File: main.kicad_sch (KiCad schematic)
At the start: 11 parts, among them J101 Conn_Coaxial, U101 SA818V

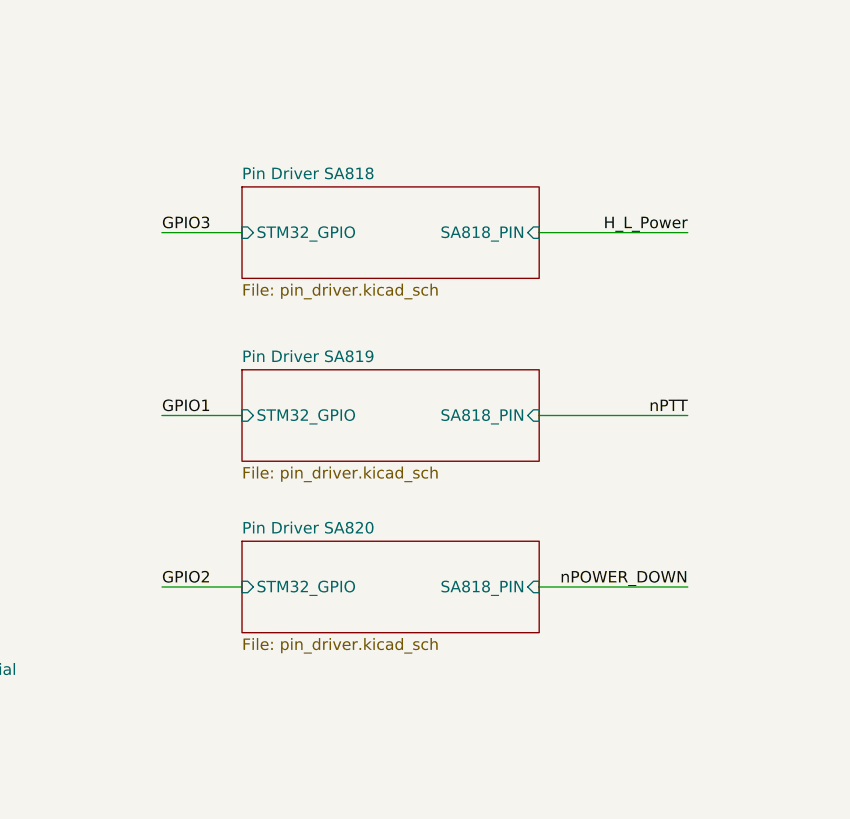
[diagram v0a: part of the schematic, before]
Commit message: update stm32, add some new 3d files
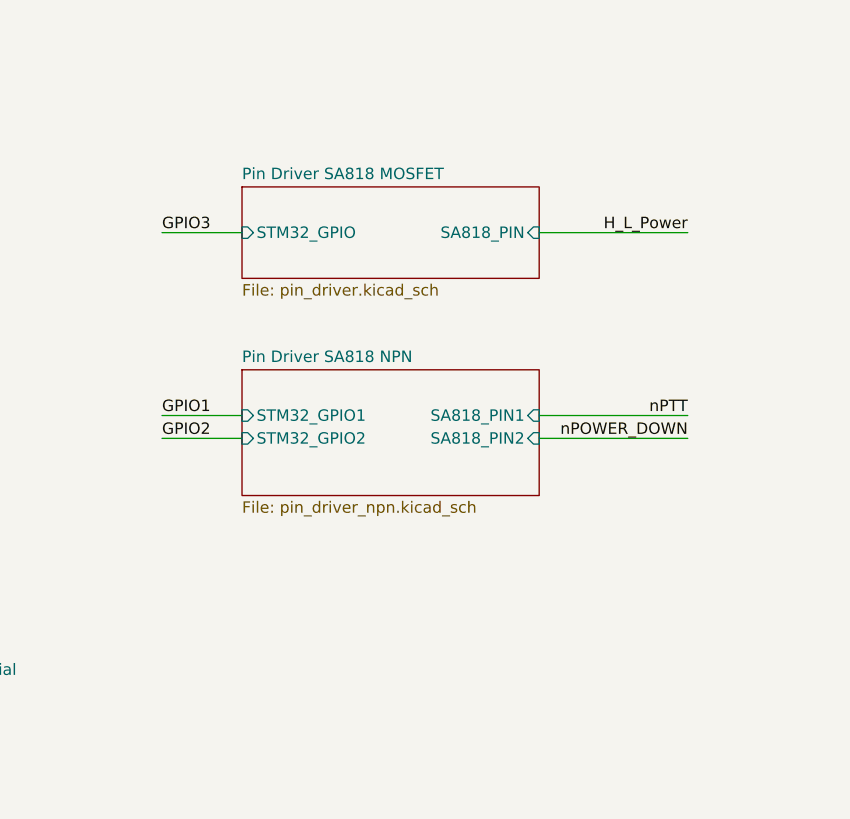
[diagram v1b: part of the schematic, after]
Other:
- sheet Pin Driver SA818 renamed Pin Driver SA818 MOSFET
- removed sheet Pin Driver SA819
- removed sheet Pin Driver SA820
- added sheet Pin Driver SA818 NPN (pin_driver_npn.kicad_sch)
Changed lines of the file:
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@@
 	(wire
 		(pts
-			(xy 158.75 144.78) (xy 175.26 144.78)
+			(xy 158.75 128.27) (xy 175.26 128.27)
 		)
 		(stroke
@@
 	(wire
 		(pts
-			(xy 116.84 144.78) (xy 125.73 144.78)
+			(xy 116.84 128.27) (xy 125.73 128.27)
 		)
 		(stroke
@@
 	)
 	(label "nPOWER_DOWN"
-		(at 175.26 144.78 180)
+		(at 175.26 128.27 180)
 		(effects
 			(font
@@
 	)
 	(label "GPIO2"
-		(at 116.84 144.78 0)
+		(at 116.84 128.27 0)
 		(effects
 			(font
@@
 	)
 	(sheet
-		(at 125.73 139.7)
-		(size 33.02 10.16)
-		(exclude_from_sim no)
-		(in_bom yes)
-		(on_board yes)
-		(dnp no)
-		(fields_autoplaced yes)
-		(stroke
-			(width 0.1524)
-			(type solid)
-		)
-		(fill
-			(color 0 0 0 0.0000)
-		)
-		(property "Sheetname" "Pin Driver SA820"
-			(at 125.73 138.9884 0)
-			(effects
-				(font
-					(size 1.27 1.27)
-				)
-				(justify left bottom)
-			)
-		)
-		(property "Sheetfile" "pin_driver.kicad_sch"
-			(at 125.73 150.4446 0)
-			(effects
-				(font
-					(size 1.27 1.27)
-				)
-				(justify left top)
-			)
-		)
-		(pin "SA818_PIN" input
-			(at 158.75 144.78 0)
-			(effects
-				(font
-					(size 1.27 1.27)
-				)
-				(justify right)
-			)
-		)
-		(pin "STM32_GPIO" input
-			(at 125.73 144.78 180)
-			(effects
-				(font
-					(size 1.27 1.27)
-				)
-				(justify left)
-			)
-		)
-		(instances
-			(project "fm"
-				(path "/f228839c-6576-40b2-ae70-679b7b460639"
-					(page "7")
-				)
-			)
-		)
-	)
-	(sheet
 		(at 125.73 100.33)
 		(size 33.02 10.16)
@@
 			(color 0 0 0 0.0000)
 		)
-		(property "Sheetname" "Pin Driver SA818"
+		(property "Sheetname" "Pin Driver SA818 MOSFET"
 			(at 125.73 99.6184 0)
 			(effects
@@
 		)
 		(instances
-			(project "fm"
+			(project "main"
 				(path "/f228839c-6576-40b2-ae70-679b7b460639"
 					(page "5")
@@
 		)
 		(instances
-			(project "fm"
+			(project "main"
 				(path "/f228839c-6576-40b2-ae70-679b7b460639"
 					(page "4")
@@
 	(sheet
 		(at 125.73 120.65)
-		(size 33.02 10.16)
+		(size 33.02 13.97)
 		(exclude_from_sim no)
 		(in_bom yes)
@@
 			(color 0 0 0 0.0000)
 		)
-		(property "Sheetname" "Pin Driver SA819"
+		(property "Sheetname" "Pin Driver SA818 NPN"
 			(at 125.73 119.9384 0)
 			(effects
@@
 			)
 		)
-		(property "Sheetfile" "pin_driver.kicad_sch"
-			(at 125.73 131.3946 0)
+		(property "Sheetfile" "pin_driver_npn.kicad_sch"
+			(at 125.73 135.2046 0)
 			(effects
 				(font
@@
 			)
 		)
-		(pin "SA818_PIN" input
+		(pin "SA818_PIN1" input
 			(at 158.75 125.73 0)
 			(effects
@@
 			)
 		)
-		(pin "STM32_GPIO" input
+		(pin "SA818_PIN2" input
+			(at 158.75 128.27 0)
+			(effects
+				(font
+					(size 1.27 1.27)
+				)
+				(justify right)
+			)
+		)
+		(pin "STM32_GPIO1" input
 			(at 125.73 125.73 180)
 			(effects
@@
 			)
 		)
-		(instances
-			(project "fm"
-				(path "/f228839c-6576-40b2-ae70-679b7b460639"
-					(page "6")
+		(pin "STM32_GPIO2" input
+			(at 125.73 128.27 180)
+			(effects
+				(font
+					(size 1.27 1.27)
+				)
+				(justify left)
+			)
+		)
+		(instances
+			(project "main"
+				(path "/f228839c-6576-40b2-ae70-679b7b460639"
+					(page "7")
 				)
 			)
@@
 		)
 		(instances
-			(project "fm"
+			(project "main"
 				(path "/f228839c-6576-40b2-ae70-679b7b460639"
 					(page "8")
@@
 		)
 		(instances
-			(project "fm"
+			(project "main"
 				(path "/f228839c-6576-40b2-ae70-679b7b460639"
 					(page "3")
@@
 		)
 		(instances
-			(project "fm"
+			(project "main"
 				(path "/f228839c-6576-40b2-ae70-679b7b460639"
 					(page "2")

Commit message: add mouser part numbers
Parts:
- C102: MOUSER 963-EMK212BJ106KG-T -> 963-EMK212BJ106KG-T
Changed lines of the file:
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@@
+			)
+		)
+		(property "SnapEDA_Link" ""
+			(at 213.36 52.07 90)
+			(effects
+				(font
+					(size 1.27 1.27)
+				)
+				(hide yes)
 			)
 		)
@@
 			)
 		)
+		(property "SnapEDA_Link" ""
+			(at 17.78 184.15 0)
+			(effects
+				(font
+					(size 1.27 1.27)
+				)
+				(hide yes)
+			)
+		)
 		(instances
 			(project "fm"
@@
 			)
 		)
+		(property "SnapEDA_Link" ""
+			(at 58.42 152.4 0)
+			(effects
+				(font
+					(size 1.27 1.27)
+				)
+				(hide yes)
+			)
+		)
 		(pin "1"
 		)
@@
 			)
 		)
+		(property "SnapEDA_Link" ""
+			(at 199.39 71.12 0)
+			(effects
+				(font
+					(size 1.27 1.27)
+				)
+				(hide yes)
+			)
+		)
 		(pin "1"
 		)
@@
 			)
 		)
+		(property "SnapEDA_Link" ""
+			(at 60.96 85.09 0)
+			(effects
+				(font
+					(size 1.27 1.27)
+				)
+				(hide yes)
+			)
+		)
 		(pin "5"
 		)
@@
 			)
 		)
+		(property "SnapEDA_Link" ""
+			(at 222.25 49.53 90)
+			(effects
+				(font
+					(size 1.27 1.27)
+				)
+				(hide yes)
+			)
+		)
 		(pin "2"
 		)
@@
 			)
 		)
+		(property "SnapEDA_Link" ""
+			(at 85.09 152.4 0)
+			(effects
+				(font
+					(size 1.27 1.27)
+				)
+				(hide yes)
+			)
+		)
 		(pin "2"
 		)
@@
 			)
 		)
+		(property "SnapEDA_Link" ""
+			(at 17.78 190.5 0)
+			(effects
+				(font
+					(size 1.27 1.27)
+				)
+				(hide yes)
+			)
+		)
 		(instances
 			(project "fm"
@@
 			)
 		)
+		(property "SnapEDA_Link" ""
+			(at 207.01 64.77 0)
+			(effects
+				(font
+					(size 1.27 1.27)
+				)
+				(hide yes)
+			)
+		)
 		(pin "2"
 		)
@@
 			)
 		)
+		(property "SnapEDA_Link" ""
+			(at 29.21 34.29 0)
+			(effects
+				(font
+					(size 1.27 1.27)
+				)
+				(hide yes)
+			)
+		)
 		(pin "1"
 		)
@@
 			)
 		)
-		(property "MOUSER" "963-EMK212BJ106KG-T "
+		(property "MOUSER" "963-EMK212BJ106KG-T"
 			(at 44.45 34.29 0)
 			(effects
+				(font
+					(size 1.27 1.27)
+				)
+				(hide yes)
+			)
+		)
+		(property "SnapEDA_Link" ""
+			(at 44.45 34.29 0)
+			(effects
